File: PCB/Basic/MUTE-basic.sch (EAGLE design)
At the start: 29 parts, among them IC1 REG1117, U1 SILICON_LABS-MICROCONTROLLER-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

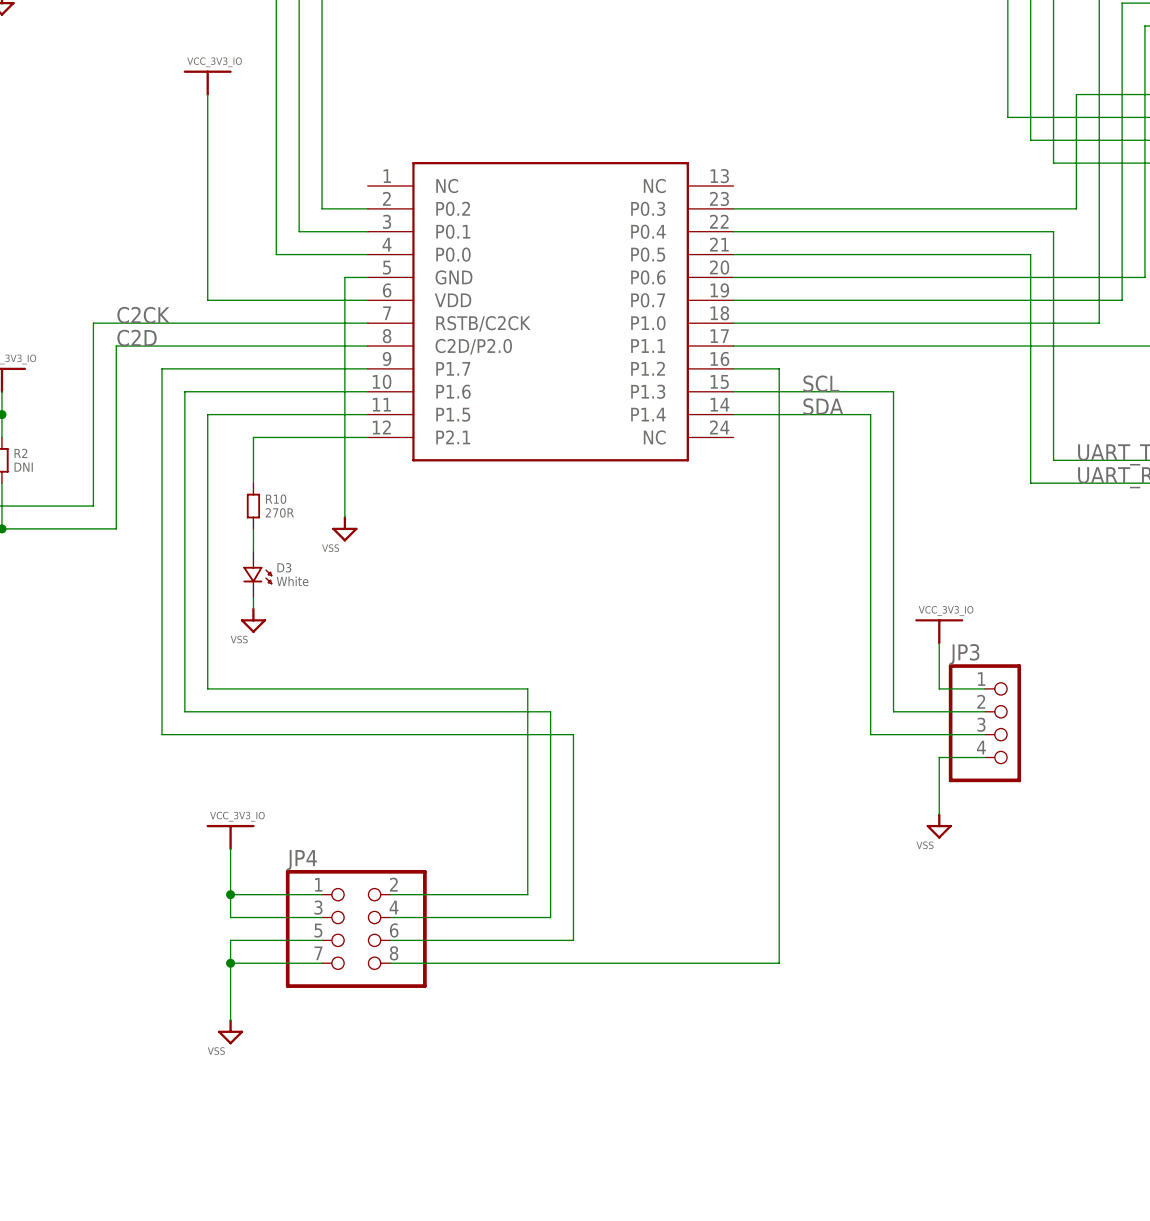
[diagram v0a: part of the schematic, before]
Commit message: Updated MCU to SOIC16 version for availability
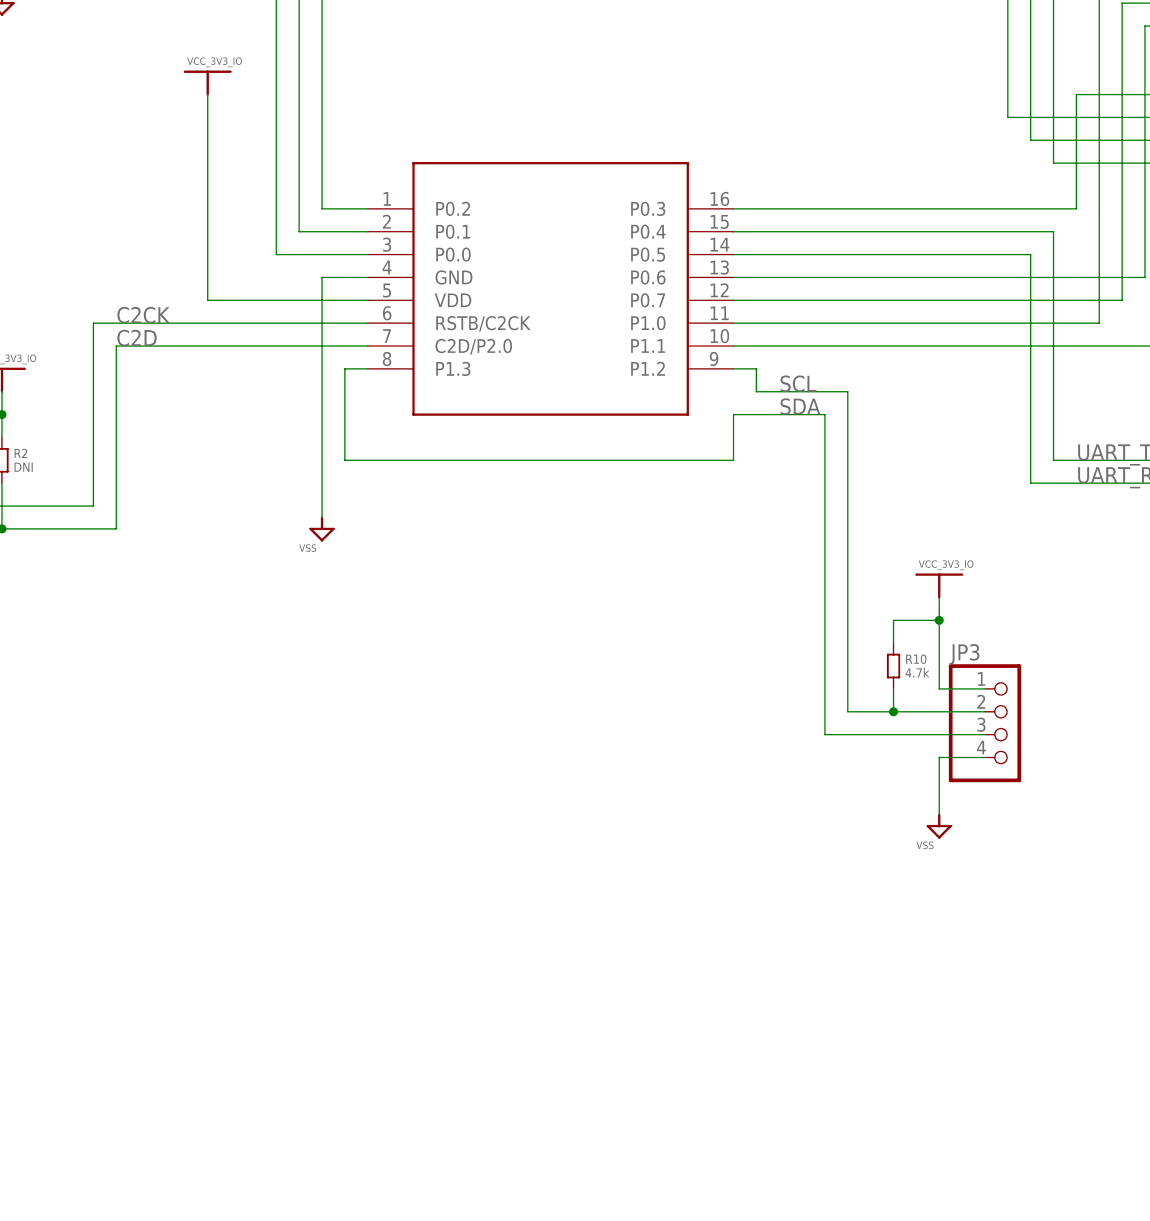
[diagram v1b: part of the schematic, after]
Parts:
- removed D3: White, standardparts:LED.0603
- removed JP4: (no value), pinhead:PINHD-2X4
- R10: value 270R -> 4.7k
- U1: value SILICON_LABS-MICROCONTROLLER-EFM8BB1X -> SILICON_LABS-MICROCONTROLLER-EFM8BB10F8G-SOIC16; device Module_ICs:SILICON_LABS-MICROCONTROLLER-EFM8BB1X -> Module_ICs:SILICON_LABS-MICROCONTROLLER-EFM8BB10F8G-SOIC16
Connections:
- removed net N$1: D3.1, R10.2
- removed net N$10: JP4.2, U1.P1.5
- removed net N$12: JP4.4, U1.P1.6
- removed net N$3: JP4.8, U1.P1.2
- removed net N$5: JP4.6, U1.P1.7
- removed net TEST_LED: R10.1, U1.P2.1
- net SCL: now also R10.2, U1.P1.2; no longer U1.P1.3
- net SDA: now also U1.P1.3; no longer U1.P1.4
- net VCC_3V3_IO: now also R10.1; no longer JP4.1, JP4.3
- net VSS: no longer D3.2, JP4.5, JP4.7
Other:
- moved on the sheet: R10
